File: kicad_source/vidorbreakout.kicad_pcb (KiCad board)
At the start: 2 copper layers, 39 x 46 mm, 14 parts, among them CN1 TE_2041119-2, CN2 CONN_01X18, CN3 CONN_01X18

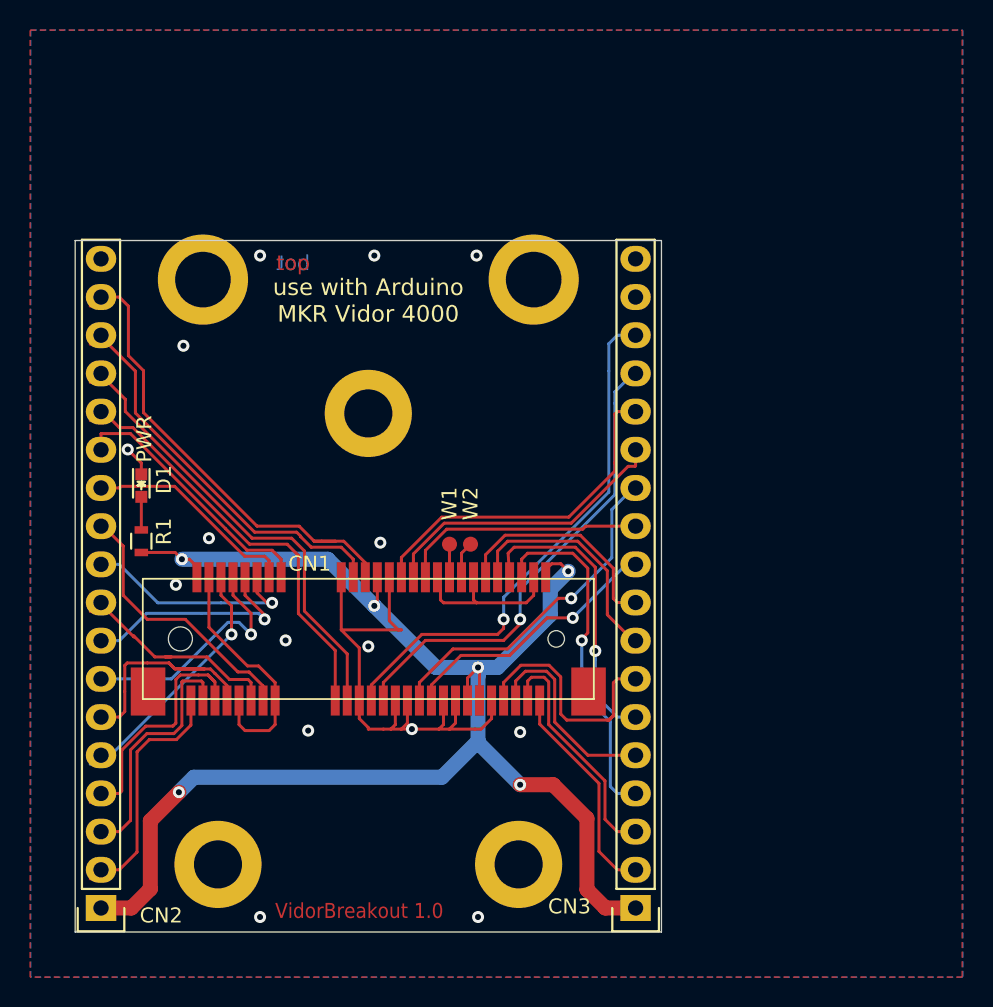
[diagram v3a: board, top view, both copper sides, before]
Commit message: added license information in schematic and layout, improved silkscreen
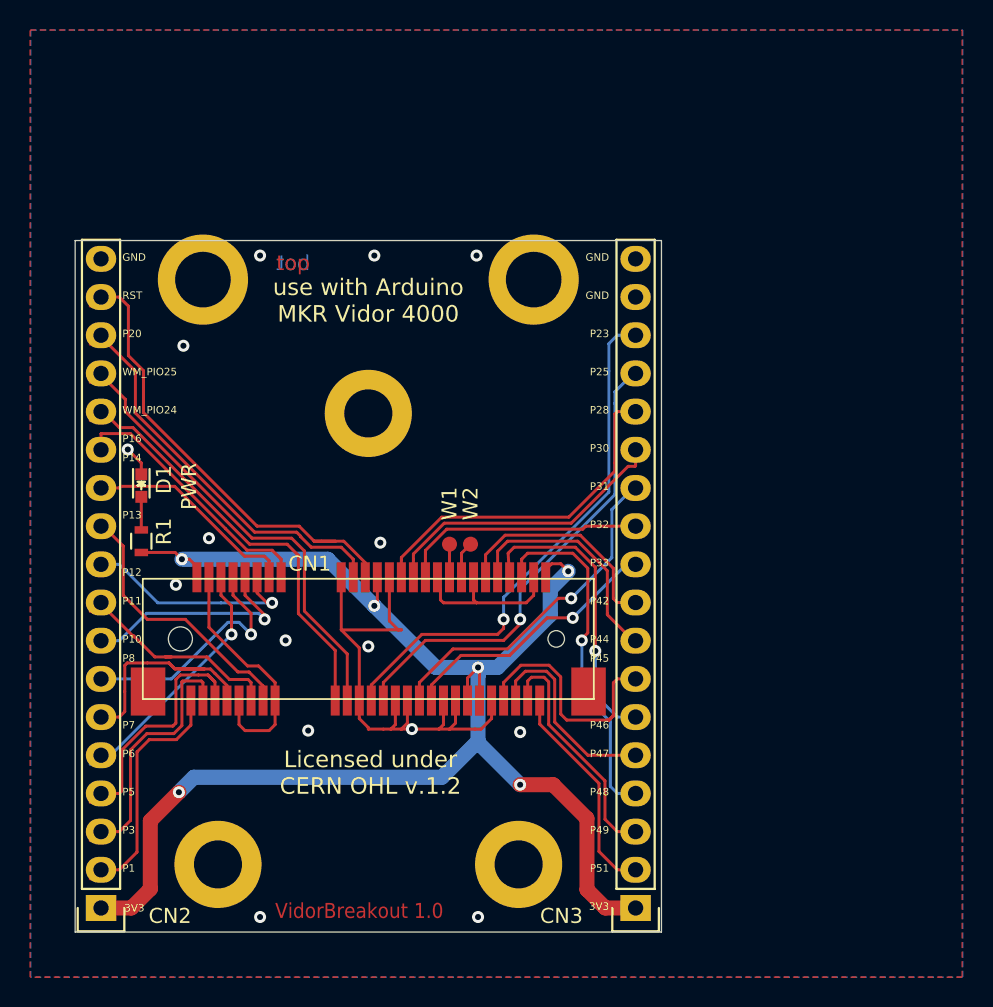
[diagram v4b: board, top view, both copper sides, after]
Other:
- board text added: "Copyright generationmake 2020 see full project documentation at https://github.com/generationmake/VidorBreakout This documentation describes Open Hardware and is licensed under the CERN OHL v. 1.2. You may redistribute and modify this documentation under the terms of the CERN OHL v.1.2. (http://ohwr.org/cernohl). This documentation is distributed WITHOUT ANY EXPRESS OR IMPLIED WARRANTY, INCLUDING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"
- board text added: "Licensed under CERN OHL v.1.2"
- board text added: "P10"
- board text added: "P11"
- board text added: "P12"
- board text added: "P13"
- board text added: "P14"
- board text added: "P16"
- board text added: "P20"
- board text added: "P23"
- board text added: "P25"
- board text added: "P28"
- board text added: "P30"
- board text added: "P31"
- board text added: "P32"
- board text added: "P33"
- board text added: "P42"
- board text added: "P44"
- board text added: "P45"
- board text added: "P46"
- board text added: "P47"
- board text added: "P48"
- board text added: "P49"
- board text added: "P51"
- board text added: "P6"
- board text added: "P8"
- board text added: "RST"
- board text added: "visit www.generationmake.de for more information!"
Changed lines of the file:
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@@
   (general
     (thickness 1.6)
-    (drawings 47)
+    (drawings 86)
     (tracks 422)
     (zones 0)
@@
     (descr "Through hole pin header")
     (tags "pin header")
-    (fp_text reference CN2 (at -4 -0.5) (layer F.SilkS)
+    (fp_text reference CN2 (at -4.59 -0.53) (layer F.SilkS)
       (effects (font (size 1 1) (thickness 0.15)))
     )
@@
     (descr "Through hole pin header")
     (tags "pin header")
-    (fp_text reference CN3 (at 4.4 0.1) (layer F.SilkS)
+    (fp_text reference CN3 (at 4.935 -0.53) (layer F.SilkS)
       (effects (font (size 1 1) (thickness 0.15)))
     )
@@
     (pad 1 thru_hole circle (at 0 0) (size 5.8 5.8) (drill 3.2) (layers *.Cu *.Mask))
   )
+  (gr_text "visit www.generationmake.de\n for more information!" (at 100.86 119.855 90) (layer B.SilkS)
+    (effects (font (size 1 1) (thickness 0.25)) (justify mirror))
+  )
+  (gr_text "Licensed under \nCERN OHL v.1.2" (at 95.145 138.905) (layer F.SilkS)
+    (effects (font (size 1.1 1.1) (thickness 0.275)))
+  )
+  (gr_text GND (at 111.02 104.615) (layer F.SilkS)
+    (effects (font (size 0.5 0.5) (thickness 0.125)) (justify right))
+  )
+  (gr_text GND (at 111.02 107.155) (layer F.SilkS)
+    (effects (font (size 0.5 0.5) (thickness 0.125)) (justify right))
+  )
+  (gr_text P23 (at 111.02 109.695) (layer F.SilkS)
+    (effects (font (size 0.5 0.5) (thickness 0.125)) (justify right))
+  )
+  (gr_text P25 (at 111.02 112.235) (layer F.SilkS)
+    (effects (font (size 0.5 0.5) (thickness 0.125)) (justify right))
+  )
+  (gr_text P28 (at 111.02 114.775) (layer F.SilkS)
+    (effects (font (size 0.5 0.5) (thickness 0.125)) (justify right))
+  )
+  (gr_text P30 (at 111.02 117.315) (layer F.SilkS)
+    (effects (font (size 0.5 0.5) (thickness 0.125)) (justify right))
+  )
+  (gr_text P31 (at 111.02 119.855) (layer F.SilkS)
+    (effects (font (size 0.5 0.5) (thickness 0.125)) (justify right))
+  )
+  (gr_text P32 (at 111.02 122.395) (layer F.SilkS)
+    (effects (font (size 0.5 0.5) (thickness 0.125)) (justify right))
+  )
+  (gr_text P33 (at 111.02 124.935) (layer F.SilkS)
+    (effects (font (size 0.5 0.5) (thickness 0.125)) (justify right))
+  )
+  (gr_text P42 (at 111.02 127.475) (layer F.SilkS)
+    (effects (font (size 0.5 0.5) (thickness 0.125)) (justify right))
+  )
+  (gr_text P44 (at 111.02 130.015) (layer F.SilkS)
+    (effects (font (size 0.5 0.5) (thickness 0.125)) (justify right))
+  )
+  (gr_text P45 (at 111.02 131.285) (layer F.SilkS)
+    (effects (font (size 0.5 0.5) (thickness 0.125)) (justify right))
+  )
+  (gr_text P46 (at 111.02 135.73) (layer F.SilkS)
+    (effects (font (size 0.5 0.5) (thickness 0.125)) (justify right))
+  )
+  (gr_text P47 (at 111.02 137.635) (layer F.SilkS)
+    (effects (font (size 0.5 0.5) (thickness 0.125)) (justify right))
+  )
+  (gr_text P48 (at 111.02 140.175) (layer F.SilkS)
+    (effects (font (size 0.5 0.5) (thickness 0.125)) (justify right))
+  )
+  (gr_text P49 (at 111.02 142.715) (layer F.SilkS)
+    (effects (font (size 0.5 0.5) (thickness 0.125)) (justify right))
+  )
+  (gr_text P51 (at 111.02 145.255) (layer F.SilkS)
+    (effects (font (size 0.5 0.5) (thickness 0.125)) (justify right))
+  )
+  (gr_text 3V3 (at 111.02 147.795) (layer F.SilkS)
+    (effects (font (size 0.5 0.5) (thickness 0.125)) (justify right))
+  )
+  (gr_text 3V3 (at 78.77 147.9) (layer F.SilkS)
+    (effects (font (size 0.5 0.5) (thickness 0.125)) (justify left))
+  )
+  (gr_text P1 (at 78.635 145.255) (layer F.SilkS)
+    (effects (font (size 0.5 0.5) (thickness 0.125)) (justify left))
+  )
+  (gr_text P3 (at 78.635 142.715) (layer F.SilkS)
+    (effects (font (size 0.5 0.5) (thickness 0.125)) (justify left))
+  )
+  (gr_text P5 (at 78.635 140.175) (layer F.SilkS)
+    (effects (font (size 0.5 0.5) (thickness 0.125)) (justify left))
+  )
+  (gr_text P6 (at 78.635 137.635) (layer F.SilkS)
+    (effects (font (size 0.5 0.5) (thickness 0.125)) (justify left))
+  )
+  (gr_text P7 (at 78.635 135.73) (layer F.SilkS)
+    (effects (font (size 0.5 0.5) (thickness 0.125)) (justify left))
+  )
+  (gr_text P8 (at 78.635 131.285) (layer F.SilkS)
+    (effects (font (size 0.5 0.5) (thickness 0.125)) (justify left))
+  )
+  (gr_text P10 (at 78.635 130.015) (layer F.SilkS)
+    (effects (font (size 0.5 0.5) (thickness 0.125)) (justify left))
+  )
+  (gr_text P11 (at 78.635 127.475) (layer F.SilkS)
+    (effects (font (size 0.5 0.5) (thickness 0.125)) (justify left))
+  )
+  (gr_text P12 (at 78.635 125.57) (layer F.SilkS)
+    (effects (font (size 0.5 0.5) (thickness 0.125)) (justify left))
+  )
+  (gr_text P14 (at 78.635 117.95) (layer F.SilkS)
+    (effects (font (size 0.5 0.5) (thickness 0.125)) (justify left))
+  )
+  (gr_text P13 (at 78.635 121.76) (layer F.SilkS)
+    (effects (font (size 0.5 0.5) (thickness 0.125)) (justify left))
+  )
+  (gr_text P16 (at 78.635 116.68) (layer F.SilkS)
+    (effects (font (size 0.5 0.5) (thickness 0.125)) (justify left))
+  )
+  (gr_text WM_PIO24 (at 78.635 114.775) (layer F.SilkS)
+    (effects (font (size 0.5 0.5) (thickness 0.125)) (justify left))
+  )
+  (gr_text WM_PIO25 (at 78.635 112.235) (layer F.SilkS)
+    (effects (font (size 0.5 0.5) (thickness 0.125)) (justify left))
+  )
+  (gr_text P20 (at 78.635 109.695) (layer F.SilkS)
+    (effects (font (size 0.5 0.5) (thickness 0.125)) (justify left))
+  )
+  (gr_text GND (at 78.635 104.615) (layer F.SilkS)
+    (effects (font (size 0.5 0.5) (thickness 0.125)) (justify left))
+  )
+  (gr_text RST (at 78.635 107.155) (layer F.SilkS)
+    (effects (font (size 0.5 0.5) (thickness 0.125)) (justify left))
+  )
+  (gr_text "Copyright generationmake 2020\nsee full project documentation at \nhttps://github.com/generationmake/VidorBreakout\n\nThis   documentation   describes   Open   Hardware   and   is   licensed   \nunder   the CERN OHL v. 1.2.\nYou may redistribute and modify this documentation under the terms \nof the CERN OHL v.1.2. (http://ohwr.org/cernohl). This documentation \nis distributed WITHOUT   ANY   EXPRESS   OR   IMPLIED   WARRANTY, \nINCLUDING   OF MERCHANTABILITY,   SATISFACTORY   QUALITY   AND \nFITNESS   FOR   A PARTICULAR   PURPOSE.   Please   see   the   CERN   \nOHL   v.1.2  for   applicable conditions" (at 186.585 147.16) (layer Cmts.User)
+    (effects (font (size 1.5 1.5) (thickness 0.3)) (justify left))
+  )
   (gr_text 3V3 (at 111.02 147.795) (layer B.SilkS)
     (effects (font (size 1 1) (thickness 0.15)) (justify left mirror))
@@
     (effects (font (size 1 0.9) (thickness 0.225)) (justify left))
   )
-  (gr_text PWR (at 80.1 116.7 90) (layer F.SilkS)
+  (gr_text PWR (at 83.08 119.855 90) (layer F.SilkS)
     (effects (font (size 1 1) (thickness 0.25)))
   )
